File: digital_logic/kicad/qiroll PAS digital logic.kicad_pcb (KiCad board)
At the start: 2 copper layers, 53.3 x 45.7 mm, 43 parts, among them J1 led_sw1, J2 mode_thr_batt, J3 pas_sense, J4 brk_sense, J5 jumper, U1 14538, U2 4023, U3 4027, U4 14538, U5 L7805, U6 4081, U7 4047, U8 74VHC1G32

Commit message: trial component placement
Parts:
- removed the C11 at (131.4, 70.5)
- removed the C12 at (150.5, 55.9)
- removed C7: .1u, Capacitor_SMD:C_0603_1608Metric
- removed the J1 at (134.6, 53.3)
- removed the J5 at (133.3, 59.7)
- removed R11: 10k, Resistor_SMD:R_0603_1608Metric
- removed the U7 at (124.5, 79.4)
- removed U8: 74VHC1G32, Package_SO:TSOP-5_1.65x3.05mm_P0.95mm
- added C6: .22u, Capacitor_SMD:C_0603_1608Metric, F.Cu at (159.4, 101.0)
- added C9: 4.7u, Capacitor_SMD:C_0603_1608Metric, F.Cu at (156.8, 107.3)
- added J2: led_sw1, Connector_PinHeader_2.54mm:PinHeader_1x03_P2.54mm_Vertical, F.Cu at (137.2, 104.1)
- added J3: jumper, Connector_PinHeader_2.54mm:PinHeader_2x02_P2.54mm_Vertical, F.Cu at (137.8, 109.9)
- added U5: 4023, Package_SO:SOIC-14_3.9x8.7mm_P1.27mm, F.Cu at (147.3, 122.6)
- C10: value 0.47u -> 150u; footprint Capacitor_SMD:C_0603_1608Metric -> Capacitor_THT:CP_Radial_D10.0mm_P5.00mm
- C11: renamed from C6; value 0.47u -> .22u
- C2: value 1u -> .22u
- C3: value 0.47u -> .1u
- C4, C5: value 1u -> .1u
- C8: value 150u -> 1u; footprint Capacitor_THT:CP_Radial_D10.0mm_P5.00mm -> Capacitor_SMD:C_0603_1608Metric
- D1: value Reverse Protect Diode -> LL4150GS18
- F1: value PTC -> 0ZCJ0012FF2E
- R10: value 1.6k -> 73k
- R2: value 200k -> 73k
- R3: value 10k -> 200k
- R4: value 100k -> 392k
- R5: value 100k -> 73k
- R7: value 10k -> 1.6k
- R8: value 100k -> 200k
- R9: value 392K -> 200k
- U1: value 14538 -> CD4093B; footprint Package_SO:SOIC-16_3.9x9.9mm_P1.27mm -> Package_SO:SOIC-14_3.9x8.7mm_P1.27mm
- U2: value 4023 -> 4027; footprint Package_SO:SOIC-14_3.9x8.7mm_P1.27mm -> Package_SO:SOIC-16_3.9x9.9mm_P1.27mm
- U3: value 4027 -> CD4093B; footprint Package_SO:SOIC-16_3.9x9.9mm_P1.27mm -> Package_SO:SOIC-14_3.9x8.7mm_P1.27mm
- U4: value 14538 -> 74VHC1G32; footprint Package_SO:SOIC-16_3.9x9.9mm_P1.27mm -> Package_SO:TSOP-5_1.65x3.05mm_P0.95mm
- U6: value 4081 -> 14538; footprint Package_SO:SOIC-14_3.9x8.7mm_P1.27mm -> Package_SO:SOIC-16_3.9x9.9mm_P1.27mm
- U7: renamed from U5; value L7805 -> 78L05
- moved H1 80.0 mm to (158.8, 125.1)
- moved H2 79.8 mm to (114.3, 125.0)
- moved C1 76.8 mm to (120.7, 123.2)
- moved R1 76.1 mm to (120.7, 125.1)
- moved C8 67.1 mm to (158.8, 121.3)
- moved U1 65.9 mm to (128.3, 122.6), turned to 90 degrees
- moved R10 64.8 mm to (150.5, 109.9), turned to 180 degrees
- moved R3 59.7 mm to (150.5, 115.6), turned to 180 degrees
- moved C4 54.1 mm to (155.1, 123.2), turned to 0 degrees
- moved U6 53.9 mm to (156.2, 114.9), turned to 0 degrees
- moved J4 51.1 mm to (127.6, 104.1)
- moved J1 50.9 mm to (153.7, 104.1)
- moved J5 50.8 mm to (146.7, 104.1)
- moved C12 50.6 mm to (128.3, 110.5)
- moved R6 50.3 mm to (155.1, 121.3)
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- renumbered C9 to C12, J4 to J1, J2 to J4, J3 to J5
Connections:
- C10 pad 2: Net-(C10-Pad2) -> GND
- C11 pad 1: Net-(C6-Pad1) -> Net-(C10-Pad1)
- C13 pad 1: GND -> VCC
- C13 pad 2: VCC -> GND
- C2 pad 1: Net-(C2-Pad1) -> VCC
- C2 pad 2: GND -> Net-(C2-Pad2)
- C3 pad 1: Net-(C3-Pad1) -> GND
- C3 pad 2: GND -> Net-(C3-Pad2)
- C4 pad 1: Net-(C4-Pad1) -> VCC
- C5 pad 1: GND -> Net-(C5-Pad1)
- C5 pad 2: Net-(C5-Pad2) -> GND
- C8 pad 1: Net-(C6-Pad1) -> Net-(C8-Pad1)
- J1 pad 1: BRK -> Net-(J1-Pad1)
- J4 pad 3: Net-(J2-Pad3) -> Net-(J4-Pad3)
- J5 pad 3: Net-(J3-Pad3) -> Net-(J5-Pad3)
- R1 pad 1: VCC -> Net-(R1-Pad1)
- R10 pad 1: Net-(C6-Pad1) -> Net-(R10-Pad1)
- R10 pad 2: Net-(D1-Pad1) -> Net-(C9-Pad1)
- R2 pad 1: VCC -> Net-(J1-Pad1)
- R2 pad 2: Net-(C2-Pad1) -> GND
- R3 pad 2: Net-(J3-Pad3) -> Net-(C2-Pad2)
- R4 pad 1: VCC -> Net-(C3-Pad2)
- R4 pad 2: Net-(C5-Pad2) -> Net-(R4-Pad2)
- R5 pad 2: Net-(C3-Pad1) -> Net-(J5-Pad3)
- R6 pad 2: Net-(C4-Pad1) -> Net-(C8-Pad1)
- R7 pad 1: Net-(J1-Pad2) -> Net-(C10-Pad1)
- R7 pad 2: Net-(C5-Pad2) -> Net-(D1-Pad1)
- R8 pad 1: Net-(C10-Pad2) -> VCC
- R8 pad 2: Net-(R8-Pad2) -> Net-(C5-Pad1)
- R9 pad 1: Net-(C11-Pad2) -> VCC
- R9 pad 2: Net-(R9-Pad2) -> Net-(C9-Pad1)
- U1 pad 1: GND -> Net-(C1-Pad1)
- U1 pad 11: Net-(J3-Pad3) -> Net-(U1-Pad11)
- U1 pad 12: GND -> Net-(U1-Pad12)
- U1 pad 13: VCC -> Net-(R1-Pad1)
- U1 pad 14: Net-(C2-Pad1) -> VCC
- U1 pad 2: Net-(C1-Pad1) -> Net-(U1-Pad2)
- U1 pad 3: VCC -> Net-(R1-Pad1)
- U1 pad 4: Net-(J3-Pad3) -> Net-(U1-Pad4)
- U1 pad 5: VCC -> Net-(R1-Pad1)
- U1 pad 6: Net-(U1-Pad6) -> Net-(R1-Pad1)
- U1 pad 7: Net-(U1-Pad7) -> GND
- U1 pad 8: GND -> Net-(U1-Pad4)
- U2 pad 1: Net-(U2-Pad1) -> Net-(U1-Pad12)
- U2 pad 10: Net-(U2-Pad1) -> VCC
- U2 pad 11: BRK -> VCC
- U2 pad 12: BRK -> Net-(U2-Pad12)
- U2 pad 13: BRK -> Net-(J3-Pad2)
- U2 pad 14: VCC -> Net-(J3-Pad4)
- U2 pad 2: PEDAL -> Net-(U1-Pad9)
- U2 pad 4: Net-(U2-Pad3) -> GND
- U2 pad 5: Net-(U2-Pad5) -> VCC
- U2 pad 6: Net-(J5-Pad2) -> VCC
- U2 pad 8: PAS_ON -> GND
- U2 pad 9: Net-(R9-Pad2) -> Net-(J1-Pad1)
- U3 pad 1: PAS_ON -> Net-(C3-Pad2)
- U3 pad 10: VCC -> Net-(U2-Pad3)
- U3 pad 11: VCC -> Net-(U2-Pad12)
- U3 pad 12: PEDAL -> Net-(C9-Pad1)
- U3 pad 13: Net-(J5-Pad2) -> VCC
- U3 pad 14: Net-(J5-Pad4) -> VCC
- U3 pad 2: PAS_OFF -> Net-(C3-Pad2)
- U3 pad 3: Net-(U2-Pad3) -> Net-(U3-Pad3)
- U3 pad 4: GND -> Net-(J4-Pad3)
- U3 pad 5: VCC -> Net-(U3-Pad3)
- U3 pad 6: VCC -> Net-(U3-Pad3)
- U3 pad 8: GND -> Net-(C2-Pad2)
- U3 pad 9: BRK -> VCC
- U4 pad 1: GND -> Net-(U1-Pad10)
- U4 pad 2: Net-(C3-Pad1) -> Net-(U1-Pad11)
- U4 pad 3: VCC -> GND
- U4 pad 4: GND -> Net-(J2-Pad3)
- U4 pad 5: Net-(C5-Pad2) -> VCC
- U6 pad 1: PAS_ON -> GND
- U6 pad 10: PEDAL -> GND
- U6 pad 11: RGN_FLSH_2 -> Net-(U2-Pad3)
- U6 pad 12: PAS_OFF -> GND
- U6 pad 13: Net-(U6-Pad13) -> VCC
- U6 pad 14: VCC -> Net-(C8-Pad1)
- U6 pad 2: RGN_FLSH -> Net-(C5-Pad1)
- U6 pad 3: Net-(U6-Pad3) -> VCC
- U6 pad 4: Net-(J2-Pad3) -> Net-(J5-Pad3)
- U6 pad 5: Net-(C11-Pad2) -> VCC
- U6 pad 6: VCC -> Net-(R10-Pad1)
- U6 pad 7: GND -> Net-(U6-Pad7)
- U6 pad 8: Net-(U1-Pad6) -> GND
- U6 pad 9: Net-(U1-Pad10) -> Net-(U6-Pad9)
- U7 pad 1: Net-(C6-Pad1) -> Net-(C10-Pad1)
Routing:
- net VCC: track 270.2 -> 0.00 mm, vias 12 -> 0
- net Net-(J1-Pad2): track 86.0 -> 0.00 mm, vias 2 -> 0
- net GND: track 70.0 -> 0.00 mm, vias 17 -> 0
- net BRK: track 60.5 -> 0.00 mm, vias 4 -> 0
- net PAS_OFF: track 58.5 -> 0.00 mm, vias 6 -> 0
- net Net-(U6-Pad3): track 57.2 -> 0.00 mm, vias 4 -> 0
- net Net-(U1-Pad10): track 56.5 -> 0.00 mm, vias 2 -> 0
- net Net-(J3-Pad3): track 46.1 -> 0.00 mm
- net RGN_FLSH: track 39.6 -> 0.00 mm, vias 2 -> 0
- net Net-(U6-Pad13): track 35.0 -> 0.00 mm, vias 2 -> 0
- net PAS_ON: track 34.4 -> 0.00 mm, vias 2 -> 0
- net PEDAL: track 32.8 -> 0.00 mm, vias 4 -> 0
- net Net-(J2-Pad3): track 32.5 -> 0.00 mm
- net Net-(U2-Pad5): track 31.7 -> 0.00 mm
- net RGN_FLSH_2: track 28.9 -> 0.00 mm
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- removed copper zone on B.Cu, net GND
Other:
- board size 53.3 x 45.7 mm -> 49.5 x 33.7 mm
- net class Default: clearance 0.2 -> 0.15; trace_width 0.25 -> 0.15; via_dia 0.8 -> 0.65; via_drill 0.4 -> 0.35
- rule trace_clearance: 0.2 -> 0.15
- rule trace_min: 0.2 -> 0.15
- board text added: "batt"
- board text added: "pdl"
- board text added: "pro\std"
- board text added: "qiroll pedal assist v2 Eric Dasmalchi"
- board text added: "rgn/ mde"
- board text added: "thr"
- board text removed: "batt_in"
- board text removed: "pedal"
- board text removed: "pro/std"
- board text removed: "qiroll pedal assist v1.1 Eric Dasmalchi"
- board text removed: "rgn/ mode"
- board text removed: "throttle"

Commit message: v2 PCB for review/manufacture
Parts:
- removed U4: 74VHC1G32, Package_SO:TSOP-5_1.65x3.05mm_P0.95mm
- added J6: Jumper, Connector_PinHeader_2.54mm:PinHeader_1x02_P2.54mm_Vertical, F.Cu at (134.8, 109.2)
- added R11: 392k, Resistor_SMD:R_0603_1608Metric, F.Cu at (153.2, 125.1)
- J3: value jumper -> Jumper; footprint Connector_PinHeader_2.54mm:PinHeader_2x02_P2.54mm_Vertical -> Connector_PinHeader_2.54mm:PinHeader_1x02_P2.54mm_Vertical
- R8: value 200k -> 392k
- U5: value 4023 -> CD4093B
- U7: value 78L05 -> L78L05_TO92; footprint Package_TO_SOT_THT:TO-92 -> Package_TO_SOT_THT:TO-92_Inline
- moved R4 5.60 mm to (151.1, 119.8), turned to 270 degrees
- moved C8 4.07 mm to (155.6, 123.8), turned to 270 degrees
- moved U2 2.29 mm to (136.5, 120.7)
- moved C4 2.05 mm to (153.0, 123.2), turned to 180 degrees
- moved J3 2.01 mm to (138.4, 111.8), turned to 180 degrees
- moved U1 1.80 mm to (127.0, 121.3), turned to 0 degrees
- moved U5 1.80 mm to (146.1, 121.3)
- moved R6 1.46 mm to (153.7, 121.3)
- moved C1 1.27 mm to (119.4, 123.2), turned to 180 degrees
- moved R1 1.27 mm to (119.4, 125.1)
- moved H1 1.27 mm to (158.8, 123.8)
- moved H2 1.14 mm to (114.3, 123.8)
- moved C11 0.78 mm to (123.2, 112.4)
- moved C10 0.20 mm to (117.9, 114.3)
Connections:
- C12 pad 1: VCC -> VDD
- C13 pad 1: VCC -> VDD
- C2 pad 1: VCC -> VDD
- C4 pad 1: VCC -> GND
- C4 pad 2: GND -> VDD
- D1 pad 1: Net-(D1-Pad1) -> Net-(C10-Pad1)
- D1 pad 2: VCC -> VDD
- F1 pad 1: Net-(D1-Pad1) -> Net-(F1-Pad1)
- J1 pad 2: VCC -> VDD
- J4 pad 4: Net-(J3-Pad1) -> Net-(J3-Pad2)
- J5 pad 1: VCC -> VDD
- R3 pad 1: VCC -> VDD
- R5 pad 1: VCC -> VDD
- R6 pad 1: VCC -> VDD
- R7 pad 2: Net-(D1-Pad1) -> Net-(F1-Pad1)
- R8 pad 1: VCC -> VDD
- R9 pad 1: VCC -> VDD
- U1 pad 13: Net-(R1-Pad1) -> Net-(U1-Pad13)
- U1 pad 14: VCC -> VDD
- U1 pad 4: Net-(U1-Pad4) -> Net-(U1-Pad13)
- U1 pad 8: Net-(U1-Pad4) -> Net-(R1-Pad1)
- U2 pad 1: Net-(U1-Pad12) -> Net-(U1-Pad9)
- U2 pad 10: VCC -> VDD
- U2 pad 11: VCC -> VDD
- U2 pad 13: Net-(J3-Pad2) -> Net-(J3-Pad1)
- U2 pad 14: Net-(J3-Pad4) -> Net-(J6-Pad2)
- U2 pad 16: VCC -> VDD
- U2 pad 2: Net-(U1-Pad9) -> Net-(U1-Pad12)
- U2 pad 5: VCC -> VDD
- U2 pad 6: VCC -> VDD
- U3 pad 1: Net-(C3-Pad2) -> Net-(U1-Pad10)
- U3 pad 13: VCC -> VDD
- U3 pad 14: VCC -> VDD
- U3 pad 2: Net-(C3-Pad2) -> Net-(U1-Pad11)
- U3 pad 3: Net-(U3-Pad3) -> Net-(J2-Pad3)
- U3 pad 5: Net-(U3-Pad3) -> Net-(U3-Pad5)
- U3 pad 6: Net-(U3-Pad3) -> Net-(U3-Pad6)
- U3 pad 9: VCC -> VDD
- U5 pad 1: Net-(U5-Pad1) -> Net-(J1-Pad1)
- U5 pad 10: Net-(U5-Pad1) -> Net-(R4-Pad2)
- U5 pad 11: Net-(J1-Pad1) -> Net-(U3-Pad5)
- U5 pad 12: Net-(J1-Pad1) -> Net-(C3-Pad2)
- U5 pad 13: Net-(J1-Pad1) -> Net-(C3-Pad2)
- U5 pad 14: VCC -> VDD
- U5 pad 2: Net-(U2-Pad12) -> Net-(J1-Pad1)
- U5 pad 3: Net-(J1-Pad1) -> Net-(U3-Pad6)
- U5 pad 4: Net-(J1-Pad1) -> Net-(J3-Pad1)
- U5 pad 5: GND -> Net-(U2-Pad3)
- U5 pad 6: Net-(J3-Pad2) -> Net-(R11-Pad1)
- U5 pad 8: Net-(U1-Pad12) -> Net-(U2-Pad12)
- U5 pad 9: Net-(R4-Pad2) -> Net-(U1-Pad9)
- U6 pad 10: GND -> Net-(R11-Pad2)
- U6 pad 13: VCC -> VDD
- U6 pad 16: VCC -> VDD
- U6 pad 3: VCC -> VDD
- U6 pad 5: VCC -> VDD
- U6 pad 6: Net-(R10-Pad1) -> Net-(U6-Pad6)
- U6 pad 7: Net-(U6-Pad7) -> Net-(R10-Pad1)
- U7 pad 1: Net-(C10-Pad1) -> VDD
- U7 pad 3: VCC -> Net-(C10-Pad1)
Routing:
- net VDD: track 0.00 -> 143.3 mm, vias 0 -> 4
- net GND: track 0.00 -> 50.7 mm, vias 0 -> 15
- net Net-(U1-Pad9): track 0.00 -> 36.8 mm
- net Net-(U2-Pad12): track 0.00 -> 36.2 mm, vias 0 -> 2
- net Net-(U2-Pad3): track 0.00 -> 36.0 mm, vias 0 -> 3
- net Net-(J1-Pad1): track 0.00 -> 34.4 mm, vias 0 -> 1
- net Net-(U1-Pad11): track 0.00 -> 33.9 mm
- net Net-(C2-Pad2): track 0.00 -> 26.1 mm
- net Net-(U1-Pad10): track 0.00 -> 23.0 mm, vias 0 -> 2
- net Net-(J4-Pad3): track 0.00 -> 22.7 mm
- net Net-(J5-Pad3): track 0.00 -> 22.3 mm
- net Net-(C3-Pad2): track 0.00 -> 22.0 mm
- net Net-(C10-Pad1): track 0.00 -> 20.9 mm
- net Net-(J3-Pad2): track 0.00 -> 20.5 mm
- net Net-(R1-Pad1): track 0.00 -> 17.7 mm
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- added copper zone on B.Cu, net GND
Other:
- board size 49.5 x 33.7 mm -> 49.5 x 32.4 mm
- board text added: "J1"
- board text added: "J2"
- board text added: "J4"
- board text added: "J5"
- board text added: "JLCJLCJLCJLC"
- board text added: "pro|std"
- board text removed: "pro\std"

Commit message: add v2 gerbers, pending review
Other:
- board text removed: "batt"

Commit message: v2 PCB for production
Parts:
- R10, R2, R5: value 73k -> 75k
- R11, R4, R6, R8: value 392k -> 390k
- U1, U3, U5: value CD4093B -> 4093B
- U2: value 4027 -> 4027B
- U6: value 14538 -> 14538B
- moved C13 4.47 mm to (129.5, 114.8)
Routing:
- net Net-(J3-Pad2): track 20.5 -> 23.7 mm, vias 0 -> 1
- net Net-(C10-Pad1): track 20.9 -> 22.7 mm, vias 0 -> 1
- net GND: track 50.7 -> 52.4 mm
- net VDD: track 143.3 -> 141.7 mm
- net Net-(U2-Pad12): track 36.2 -> 35.5 mm
- net Net-(U1-Pad9): track 36.8 -> 36.1 mm
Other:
- board text added: "batt"

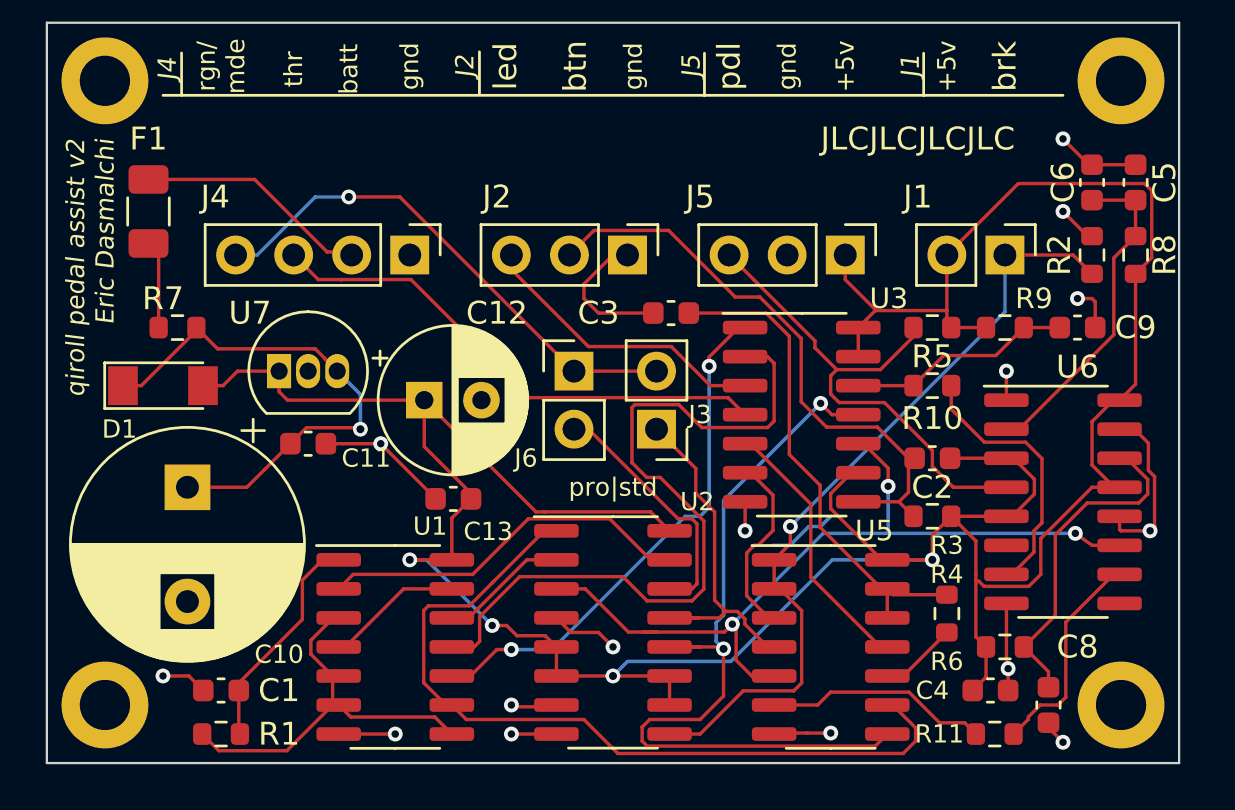
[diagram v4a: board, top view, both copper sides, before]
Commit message: pcb version 2.2, hopefully fixes brake input/mode instablity
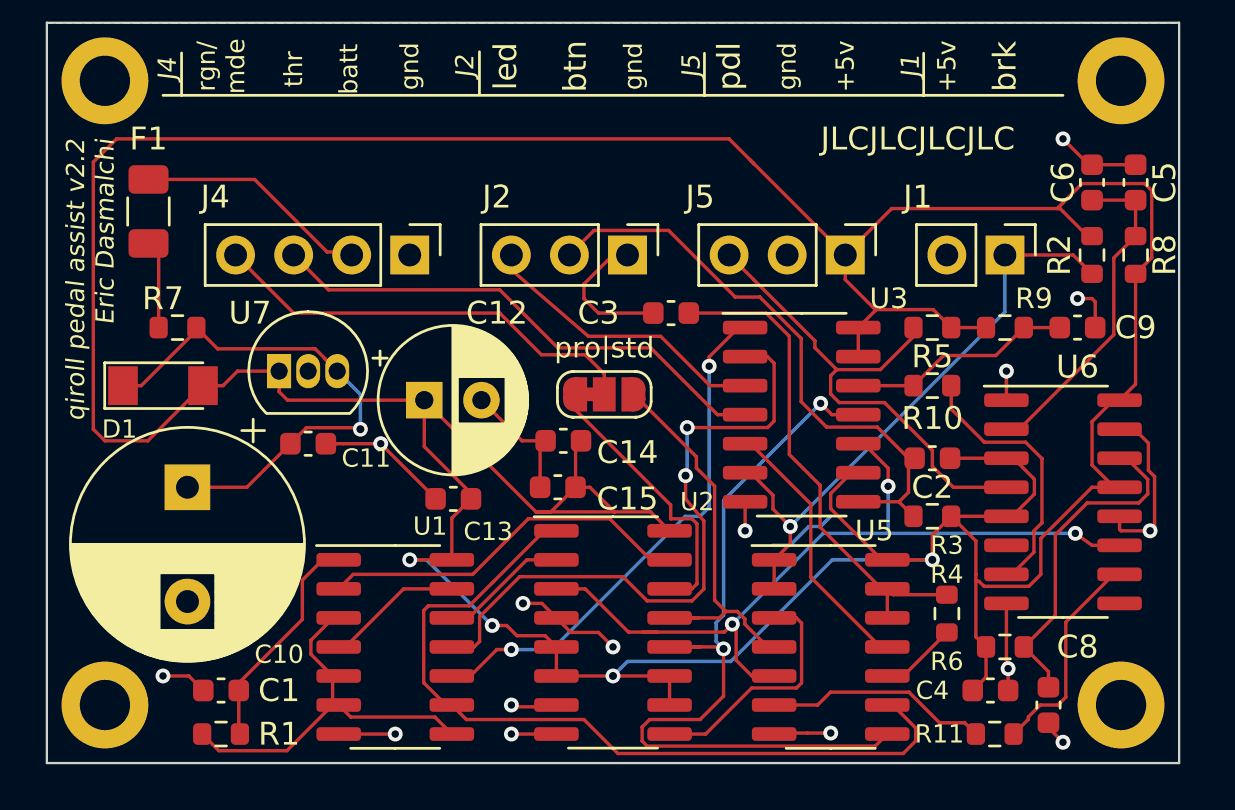
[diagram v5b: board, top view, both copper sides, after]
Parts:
- removed J3, J6: Jumper, Connector_PinHeader_2.54mm:PinHeader_1x02_P2.54mm_Vertical
- added C14: 22u, Capacitor_SMD:C_0603_1608Metric, F.Cu at (134.4, 112.3)
- added C15: 1u, Capacitor_SMD:C_0603_1608Metric, F.Cu at (134.1, 114.3)
- added JP1: SolderJumper_3_Bridged12, Jumper:SolderJumper-3_P1.3mm_Bridged12_RoundedPad1.0x1.5mm_NumberLabels, F.Cu at (136.1, 110.2)
- C12: value 200u -> 470u
- R2: value 75k -> 1.6k
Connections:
- J1 pad 2: VDD -> GND
- R2 pad 2: GND -> VDD
- U2 pad 9: Net-(J1-Pad1) -> Net-(U2-Pad9)
- U3 pad 6: Net-(U3-Pad6) -> Net-(J1-Pad1)
- U5 pad 3: Net-(U3-Pad6) -> Net-(U2-Pad9)
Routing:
- net VDD: track 141.7 -> 205.5 mm
- net Net-(U2-Pad9): track 0.00 -> 11.1 mm
- net Net-(U3-Pad6): track 8.44 -> 0.00 mm
- net Net-(J1-Pad1): track 34.4 -> 26.5 mm
- net GND: track 52.4 -> 58.1 mm
- net Net-(U1-Pad11): track 33.9 -> 28.7 mm, vias 0 -> 2
- net Net-(J4-Pad4): track 23.7 -> 19.4 mm, vias 1 -> 0
- net Net-(JP1-Pad3): track 15.3 -> 17.3 mm
- net Net-(JP1-Pad1): track 11.3 -> 12.6 mm
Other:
- board text added: "qiroll pedal assist v2.2 Eric Dasmalchi"
- board text removed: "qiroll pedal assist v2 Eric Dasmalchi"

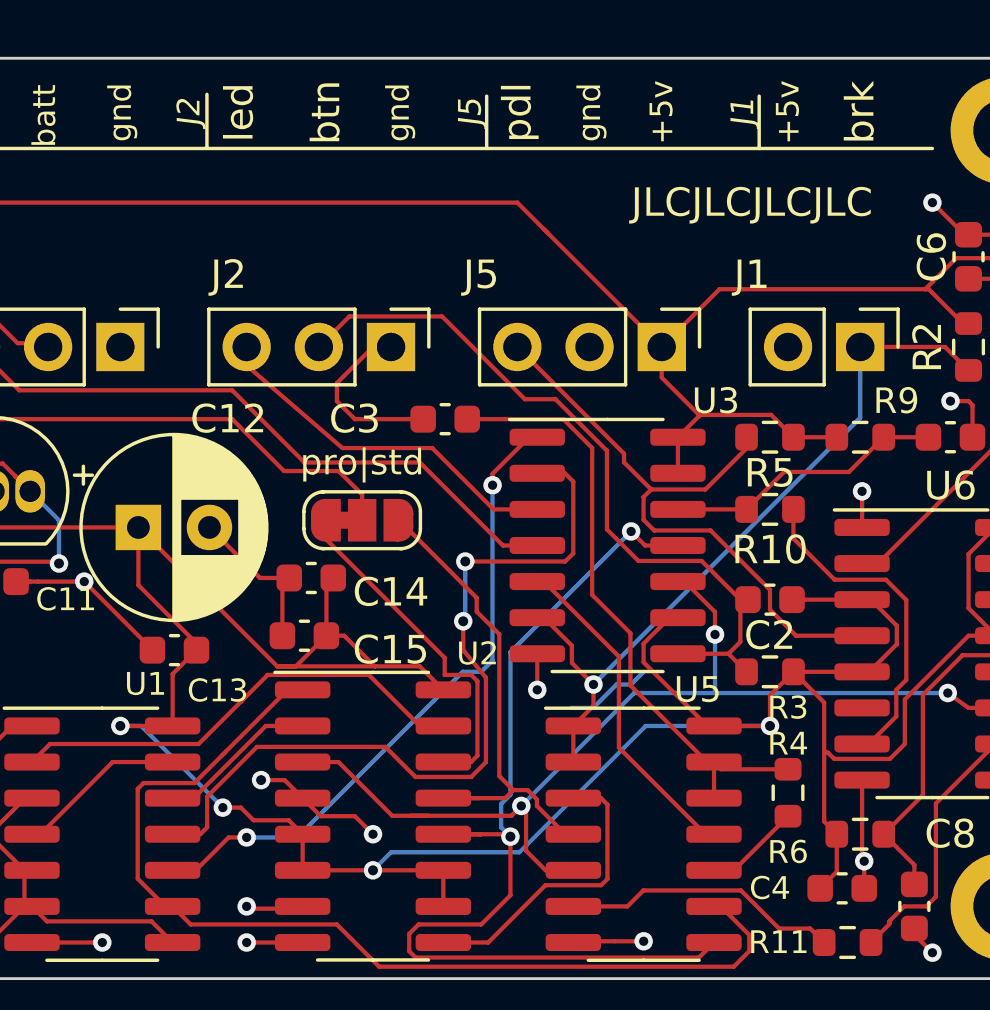
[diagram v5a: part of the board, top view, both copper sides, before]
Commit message: fix brake label, a more connected ground plane
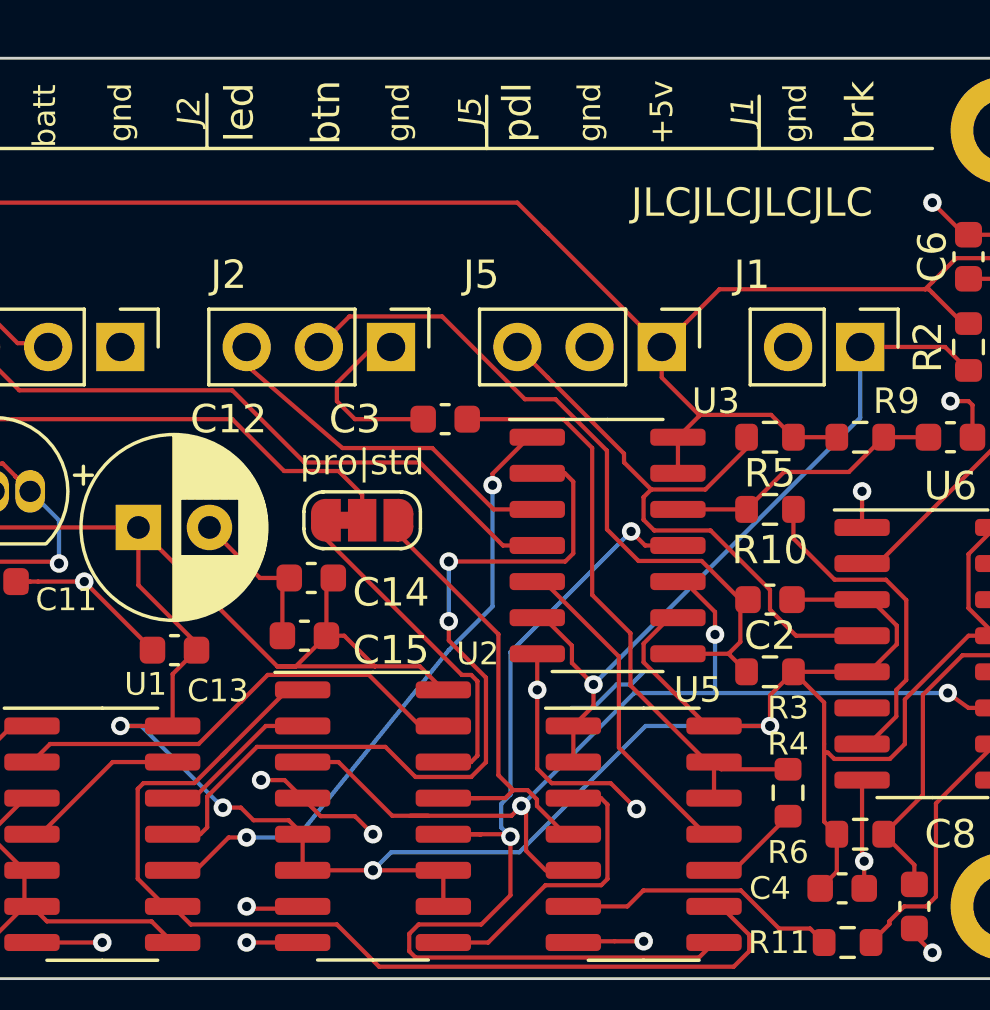
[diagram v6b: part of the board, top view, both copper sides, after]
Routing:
- net GND: track 58.1 -> 65.0 mm, vias 15 -> 16
- net Net-(U1-Pad11): track 28.7 -> 29.6 mm
- net Net-(U1-Pad10): track 23.0 -> 22.3 mm
